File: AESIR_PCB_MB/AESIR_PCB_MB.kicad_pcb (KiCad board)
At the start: 2 copper layers, 33 parts, among them J1 Umb - GND, J10 GPS - Rx, J12 Saftey Pin - 5V - IN, J13 Saftey Pin - 5V - OUT, J14 Saftey Pin - 5V, J15 Vin - +5.5V, J16 Servo - 5V, J17 Servo - GND, J18 GPS - Tx, J19 Tel - GND, J2 Go Pro - 5V, J20 Tel - Rx, J21 Tel - Tx, J3 Umb - Rx, J4 Umb - Tx, J5 Umb - 5V, J6 Go Pro - GND, J8 GPS - GND, J9 M3 Drain - Tx Video/Cam, Q1 Q_NMOS_DGS, Q2 Q_NMOS_DGS, Q3 Q_NMOS_DGS, U1 Teensy3.6, U2 MPU-9250, U3 BMP180, U4 AESIR_MOTHERBOARD_PLATE

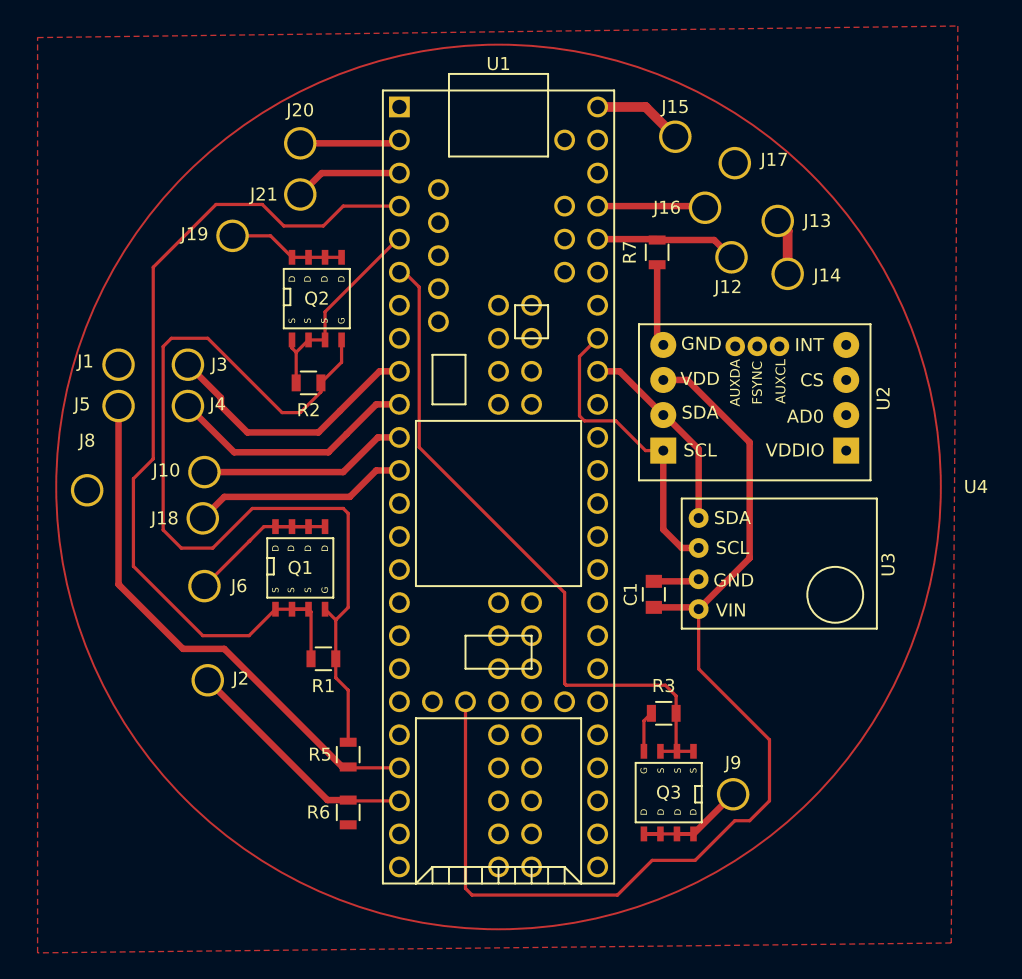
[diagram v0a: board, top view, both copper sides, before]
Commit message: finalized motherboard design, added library files
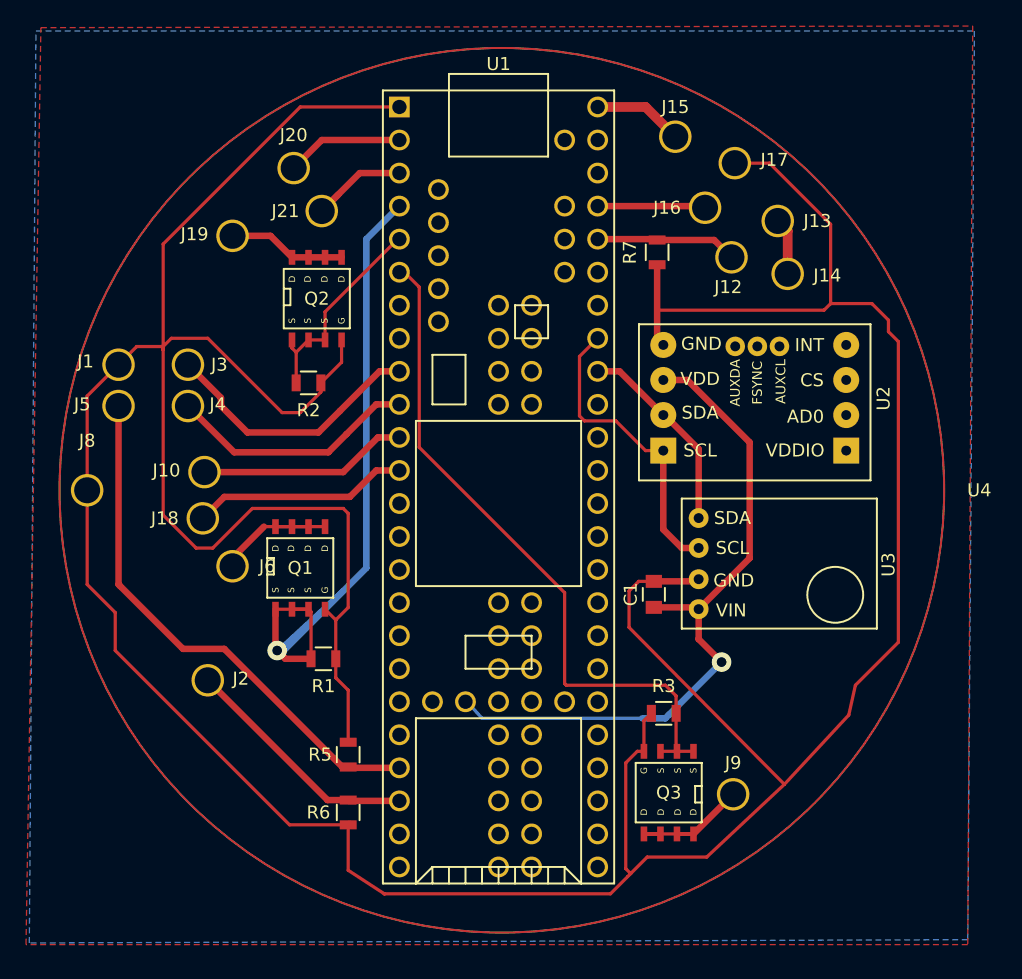
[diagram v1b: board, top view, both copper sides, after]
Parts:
- U4: footprint Enclosures:AESIR_MB_OUTLINE_68mm -> AESIR:AESIR_MB_OUTLINE_68mm
- moved J6 2.64 mm to (122.7, 101.6)
- moved J21 2.08 mm to (129.5, 74.3)
- moved J20 1.97 mm to (127.4, 71.0)
- moved U4 0.36 mm to (143.4, 95.8)
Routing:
- net GND: track 83.0 -> 311.0 mm
- net Net-(C1-Pad2): track 84.5 -> 53.9 mm, vias 0 -> 1
- net Net-(Q1-Pad2): track 67.5 -> 86.8 mm, vias 0 -> 1
- net Net-(J20-Pad1): track 7.73 -> 15.4 mm
- net Net-(J19-Pad1): track 9.07 -> 15.2 mm
- net Net-(J21-Pad1): track 8.30 -> 13.6 mm
- net Net-(J6-Pad1): track 14.1 -> 11.5 mm
- added copper zone on B.Cu, net GND

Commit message: minor update on board + added more documentation
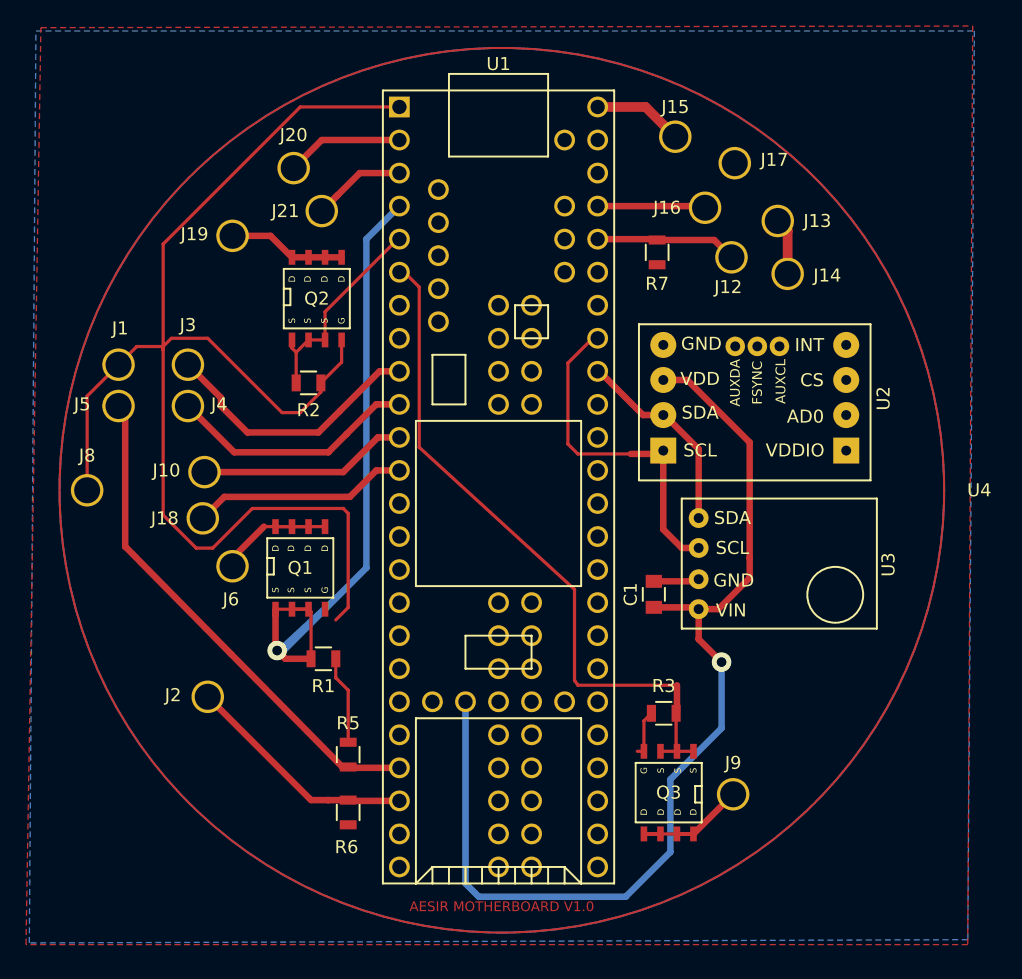
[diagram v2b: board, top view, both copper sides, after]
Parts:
- moved J2 1.27 mm to (120.8, 111.6)
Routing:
- net GND: track 311.0 -> 118.3 mm
- net Net-(C1-Pad2): track 53.9 -> 80.2 mm
- net Net-(U1-Pad46): track 23.5 -> 26.4 mm
- net Net-(J5-Pad1): track 41.2 -> 39.3 mm
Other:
- board text added: "AESIR MOTHERBOARD V1.0"
